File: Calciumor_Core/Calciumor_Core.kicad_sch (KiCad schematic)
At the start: 127 parts, among them J1 OLED, J2 USB_C_Main, Q2 2SC4116, Q3 2SC4116, SW1 SW_Push, SW10 SW_Push, SW11 SW_Push, SW12 SW_Push, SW13 SW_Push, SW14 SW_Push, SW15 SW_Push, SW16 SW_Push, SW17 SW_Push, SW18 SW_Push, SW19 TMHU27, SW2 SW_Push, SW20 Power_SW, SW21 Program, SW22 Reset, SW3 SW_Push, SW4 RotaryEncoder_Switch, SW5 SW_Push, SW6 SW_Push, SW7 SW_Push, SW8 SW_Push, SW9 SW_Push, U1 LM324APT, U2 NJM12877F25, U3 ESP32-S3-WROOM-1-N16R8, U4 MCP73831-2-OT, U5 BD5229G-1, U6 NC7SV157, U7 FT231XS, U8 XC6194AA03ER-G, U9 AE-XC9306-3V3

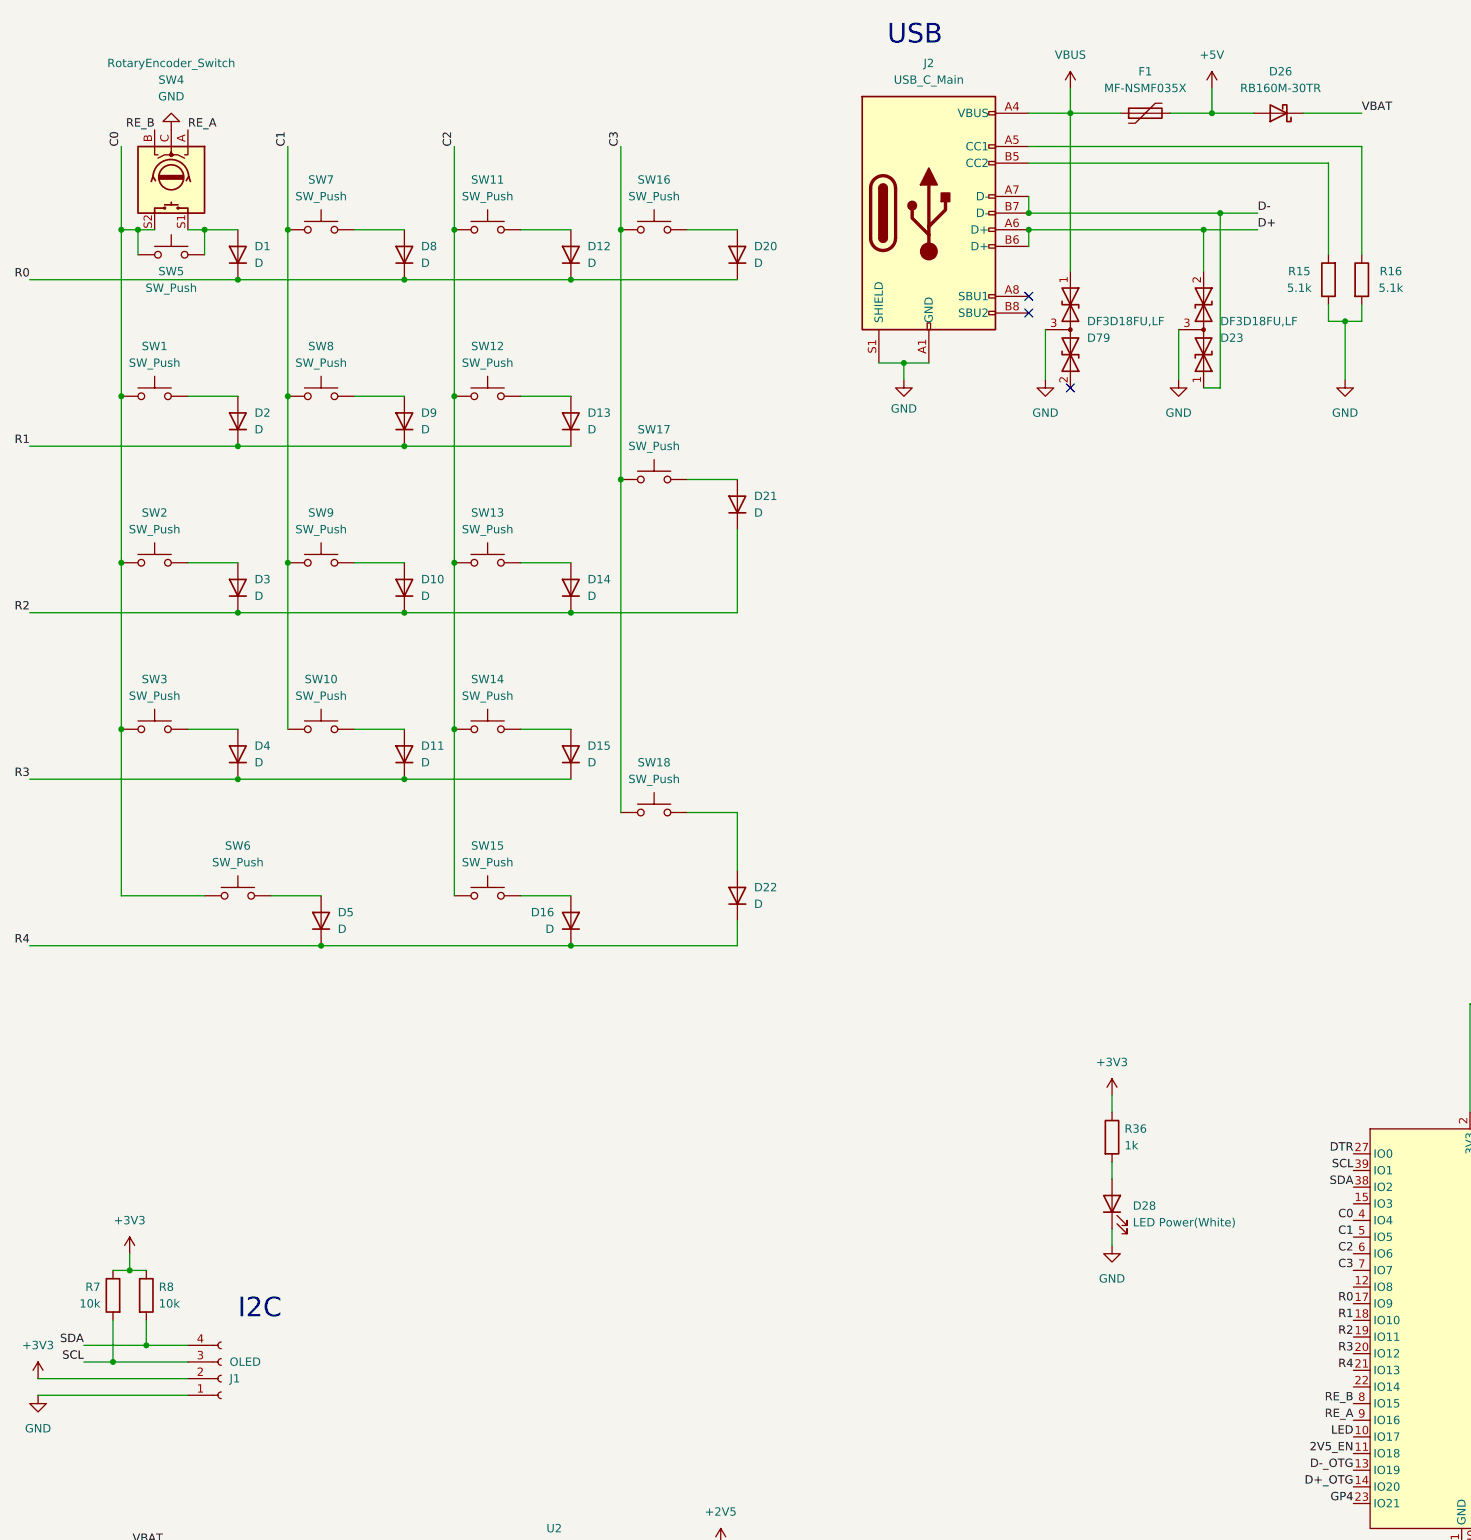
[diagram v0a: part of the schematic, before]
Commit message: Changed to socket switch type
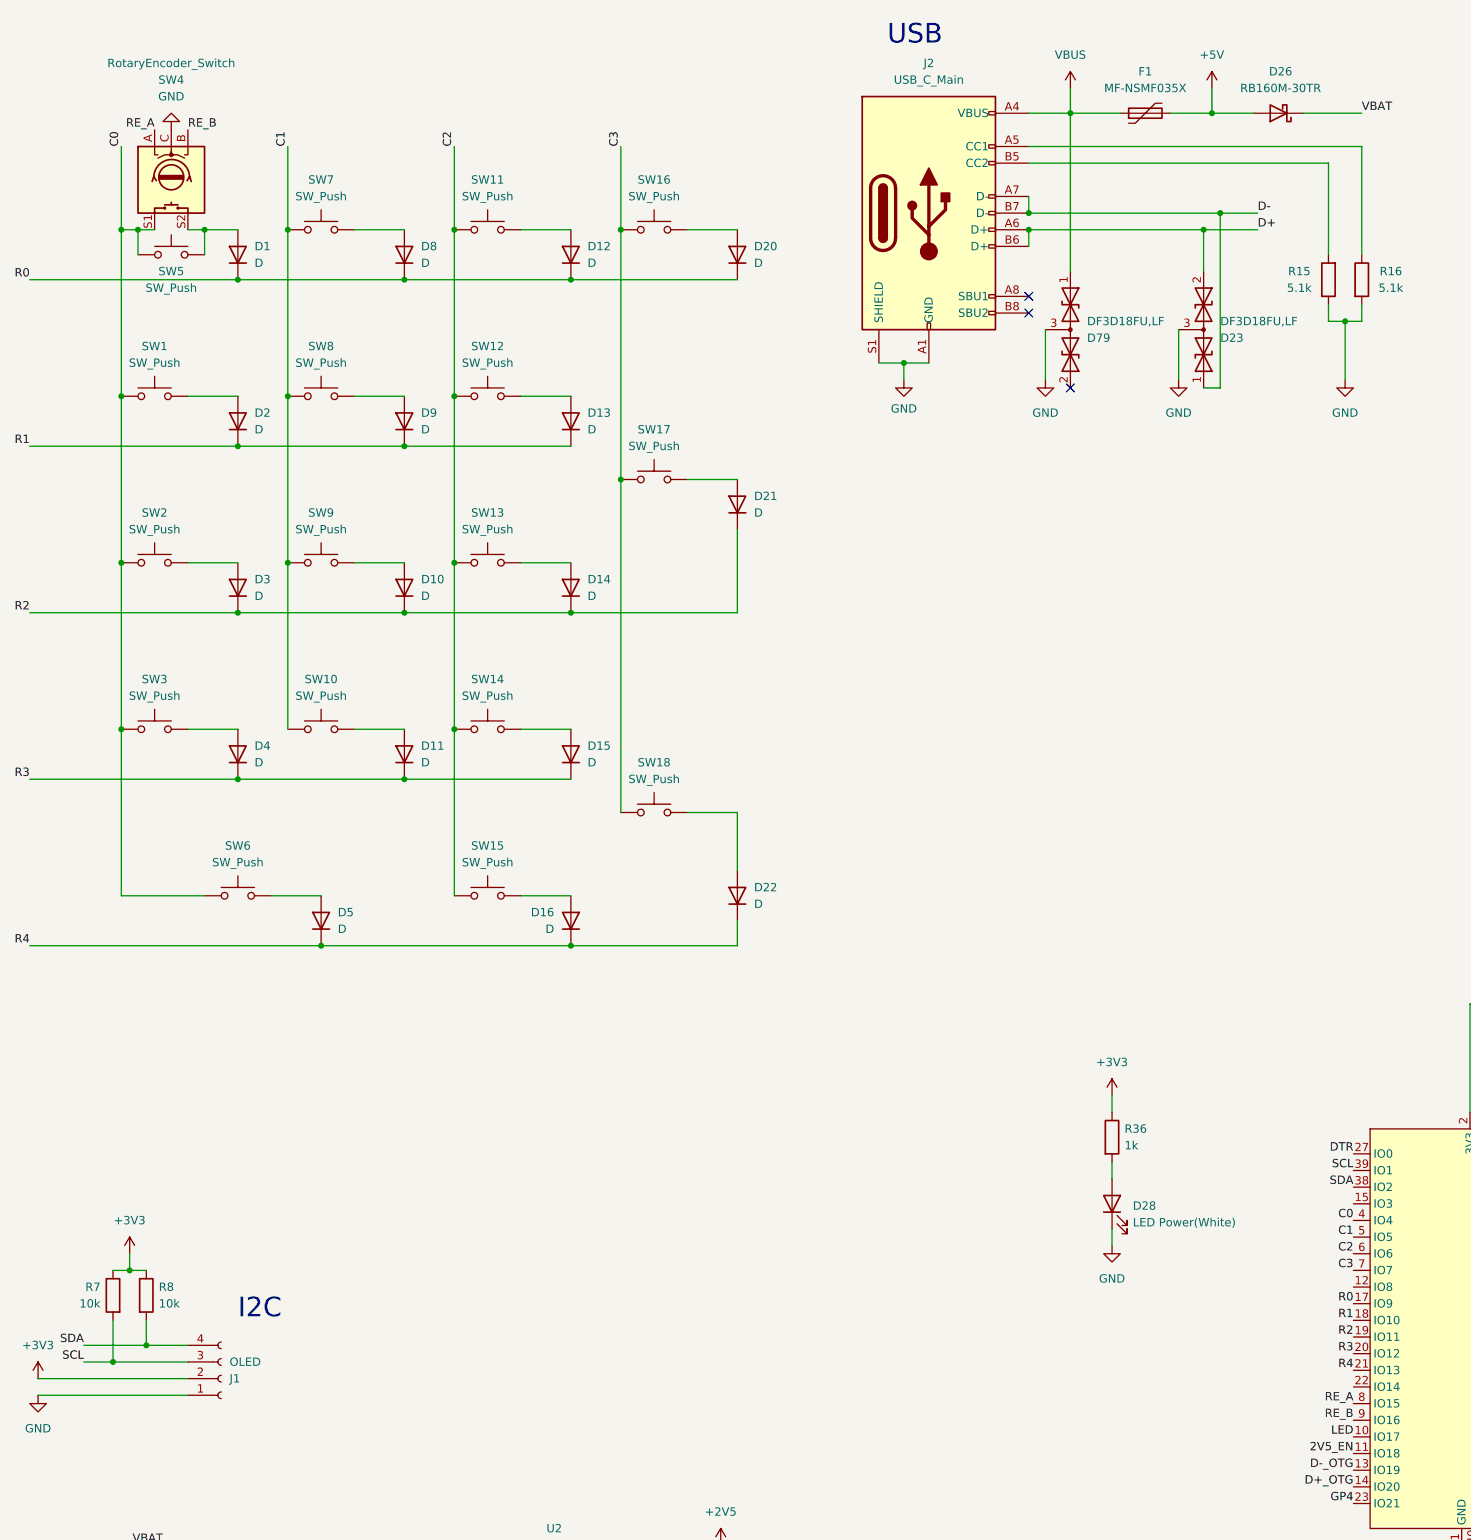
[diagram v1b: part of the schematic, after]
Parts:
- SW1, SW10, SW11, SW12, SW13, SW14, SW15, SW16, SW17, SW18, SW2, SW3, SW5, SW6, SW7, SW8, SW9: footprint Ultramarine-2:MX-Kailh -> Calciumor:MX_Choc_Socket
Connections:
- net C0: now also SW4.S1; no longer SW4.S2
- net RE_A: now also U3.8 (IO15); no longer U3.9 (IO16)
- net RE_B: now also U3.9 (IO16); no longer U3.8 (IO15)
- net at D1.2 (A), SW5.2: now also SW4.S2; no longer SW4.S1
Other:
- moved on the sheet: SW4
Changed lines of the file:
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@@
 	)
 	(label "RE_A"
-		(at 45.72 31.75 0)
+		(at 40.64 31.75 180)
 		(fields_autoplaced yes)
 		(effects
@@
 				(size 1.27 1.27)
 			)
-			(justify left bottom)
+			(justify right bottom)
 		)
 	)
@@
 	)
 	(label "RE_B"
-		(at 223.52 226.06 180)
+		(at 223.52 228.6 180)
 		(fields_autoplaced yes)
 		(effects
@@
 	)
 	(label "RE_B"
-		(at 40.64 31.75 180)
+		(at 45.72 31.75 0)
 		(fields_autoplaced yes)
 		(effects
@@
 				(size 1.27 1.27)
 			)
-			(justify right bottom)
+			(justify left bottom)
 		)
 	)
@@
 	)
 	(label "RE_A"
-		(at 223.52 228.6 180)
+		(at 223.52 226.06 180)
 		(fields_autoplaced yes)
 		(effects
@@
 			)
 		)
-		(property "Footprint" "Ultramarine-2:MX-Kailh"
+		(property "Footprint" "Calciumor:MX_Choc_Socket"
 			(at 91.44 118.11 0)
 			(effects
@@
 			)
 		)
-		(property "Footprint" "Ultramarine-2:MX-Kailh"
+		(property "Footprint" "Calciumor:MX_Choc_Socket"
 			(at 91.44 92.71 0)
 			(effects
@@
 			)
 		)
-		(property "Footprint" "Ultramarine-2:MX-Kailh"
+		(property "Footprint" "Calciumor:MX_Choc_Socket"
 			(at 66.04 67.31 0)
 			(effects
@@
 			)
 		)
-		(property "Footprint" "Ultramarine-2:MX-Kailh"
+		(property "Footprint" "Calciumor:MX_Choc_Socket"
 			(at 40.64 92.71 0)
 			(effects
@@
 			)
 		)
-		(property "Footprint" "Ultramarine-2:MX-Kailh"
+		(property "Footprint" "Calciumor:MX_Choc_Socket"
 			(at 40.64 67.31 0)
 			(effects
@@
 			)
 		)
-		(property "Footprint" "Ultramarine-2:MX-Kailh"
+		(property "Footprint" "Calciumor:MX_Choc_Socket"
 			(at 116.84 130.81 0)
 			(effects
@@
 			)
 		)
-		(property "Footprint" "Ultramarine-2:MX-Kailh"
+		(property "Footprint" "Calciumor:MX_Choc_Socket"
 			(at 91.44 41.91 0)
 			(effects
@@
 	(symbol
 		(lib_id "power:GND")
-		(at 43.18 31.75 180)
+		(at 43.18 31.75 0)
+		(mirror x)
 		(unit 1)
 		(exclude_from_sim no)
@@
 			)
 		)
-		(property "Footprint" "Ultramarine-2:MX-Kailh"
+		(property "Footprint" "Calciumor:MX_Choc_Socket"
 			(at 91.44 143.51 0)
 			(effects
@@
 			)
 		)
-		(property "Footprint" "Ultramarine-2:MX-Kailh"
+		(property "Footprint" "Calciumor:MX_Choc_Socket"
 			(at 116.84 41.91 0)
 			(effects
@@
 			)
 		)
-		(property "Footprint" "Ultramarine-2:MX-Kailh"
+		(property "Footprint" "Calciumor:MX_Choc_Socket"
 			(at 66.04 118.11 0)
 			(effects
@@
 			)
 		)
-		(property "Footprint" "Ultramarine-2:MX-Kailh"
+		(property "Footprint" "Calciumor:MX_Choc_Socket"
 			(at 116.84 80.01 0)
 			(effects
@@
 			)
 		)
-		(property "Footprint" "Ultramarine-2:MX-Kailh"
+		(property "Footprint" "Calciumor:MX_Choc_Socket"
 			(at 40.64 118.11 0)
 			(effects
@@
 			)
 		)
-		(property "Footprint" "Ultramarine-2:MX-Kailh"
+		(property "Footprint" "Calciumor:MX_Choc_Socket"
 			(at 53.34 143.51 0)
 			(effects
@@
 			)
 		)
-		(property "Footprint" "Ultramarine-2:MX-Kailh"
+		(property "Footprint" "Calciumor:MX_Choc_Socket"
 			(at 91.44 67.31 0)
 			(effects
@@
 			)
 		)
-		(property "Footprint" "Ultramarine-2:MX-Kailh"
+		(property "Footprint" "Calciumor:MX_Choc_Socket"
 			(at 43.18 45.72 0)
 			(effects
@@
 			)
 		)
-		(property "Footprint" "Ultramarine-2:MX-Kailh"
+		(property "Footprint" "Calciumor:MX_Choc_Socket"
 			(at 66.04 92.71 0)
 			(effects
@@
 	(symbol
 		(lib_id "Device:RotaryEncoder_Switch")
-		(at 43.18 39.37 270)
+		(at 43.18 39.37 90)
+		(mirror x)
 		(unit 1)
 		(exclude_from_sim no)
@@
 		)
 		(property "Footprint" "Ultramarine-2:EC12"
-			(at 47.244 35.56 0)
+			(at 39.116 35.56 0)
 			(effects
 				(font
@@
 		)
 		(property "Datasheet" "~"
-			(at 49.784 39.37 0)
+			(at 36.576 39.37 0)
 			(effects
 				(font
@@
 			)
 		)
-		(property "Footprint" "Ultramarine-2:MX-Kailh"
+		(property "Footprint" "Calciumor:MX_Choc_Socket"
 			(at 66.04 41.91 0)
 			(effects
